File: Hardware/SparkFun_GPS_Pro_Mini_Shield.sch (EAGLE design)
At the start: 23 parts, among them J1 USD_TINY, U1 EM406, U2 TXB0108, U3 AP2112K-3.3V

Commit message: Update file names and library
- Updated file names to follow standard
- Updated library with PROD_ID numbers
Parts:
- J1: value USD_TINY -> MICROSD_TINY; device uSD Socket temp:USD_TINY -> GPS_Pro_Mini_temp:MICROSD_TINY
- U1: value EM406 -> GP735; device SparkFun-Connectors:EM406 -> GPS_Pro_Mini_temp:GP735
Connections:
- net GND: now also U1.GND; no longer U1.GND1
- net GPS_PPS: now also U1.P_CTRL; no longer U1.1PPS
- net V_BATT: now also U1.VBAT; no longer U1.GND2
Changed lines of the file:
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@@
 </classes>
 <parts>
-<part name="J1" library="uSD Socket temp" deviceset="USD_TINY" device=""/>
+<part name="J1" library="GPS_Pro_Mini_temp" deviceset="MICROSD_TINY" device=""/>
 <part name="J2" library="SparkFun-Connectors" deviceset="M12" device="NO_SILK"/>
 <part name="J3" library="SparkFun-Connectors" deviceset="M12" device="NO_SILK"/>
@@
 <part name="GND1" library="SparkFun-Aesthetics" deviceset="GND" device=""/>
 <part name="GND2" library="SparkFun-Aesthetics" deviceset="GND" device=""/>
-<part name="U1" library="SparkFun-Connectors" deviceset="EM406" device=""/>
+<part name="U1" library="GPS_Pro_Mini_temp" deviceset="GP735" device=""/>
 <part name="J4" library="SparkFun-Connectors" deviceset="M06" device="NO_SILK_FEMALE_PTH"/>
 <part name="SUPPLY3" library="SparkFun-Aesthetics" deviceset="3.3V" device=""/>
@@
 </segment>
 <segment>
-<pinref part="U1" gate="G$1" pin="GND1"/>
+<pinref part="U1" gate="G$1" pin="GND"/>
 <wire x1="22.86" y1="88.9" x2="17.78" y2="88.9" width="0.1524" layer="91"/>
 <wire x1="17.78" y1="88.9" x2="17.78" y2="71.12" width="0.1524" layer="91"/>
@@
 </segment>
 <segment>
-<pinref part="U1" gate="G$1" pin="GND2"/>
+<pinref part="U1" gate="G$1" pin="VBAT"/>
 <wire x1="22.86" y1="78.74" x2="20.32" y2="78.74" width="0.1524" layer="91"/>
 <wire x1="20.32" y1="78.74" x2="20.32" y2="93.98" width="0.1524" layer="91"/>
@@
 <net name="GPS_PPS" class="0">
 <segment>
-<pinref part="U1" gate="G$1" pin="1PPS"/>
+<pinref part="U1" gate="G$1" pin="P_CTRL"/>
 <wire x1="22.86" y1="76.2" x2="15.24" y2="76.2" width="0.1524" layer="91"/>
 <label x="15.24" y="76.2" size="1.27" layer="95" rot="R180" xref="yes"/>

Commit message: Updated GPS label
Changed from GPS_PPS to GPS_CTRL
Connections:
- net GPS_PPS renamed GPS_CTRL
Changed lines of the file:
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@@
 </segment>
 </net>
-<net name="GPS_PPS" class="0">
+<net name="GPS_CTRL" class="0">
 <segment>
 <pinref part="U1" gate="G$1" pin="P_CTRL"/>

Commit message: Added board designer name and version number
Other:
- note added: "Alex Wende"
- note added: "v01"
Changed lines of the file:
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@@
 <wire x1="78.74" y1="53.34" x2="78.74" y2="0" width="0.1524" layer="97" style="shortdash"/>
 <wire x1="40.64" y1="53.34" x2="40.64" y2="0" width="0.1524" layer="97" style="shortdash"/>
+<text x="166.878" y="11.43" size="2.54" layer="94">Alex Wende</text>
+<text x="238.76" y="7.62" size="2.54" layer="94">v01</text>
 </plain>
 <instances>

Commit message: Design Review Changes
- Fixed SPI traces
- Moved VIN of regulator to VIN instead of RAW
- Removed jumpers for software/hardware uart with DPDT switch
- Added product name to board
- Replaced coin cell battery with two PTH pins to make the board smaller
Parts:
- removed BAT1: 12MM Coin Cell, SparkFun-Electromechanical:BATTERY12MM
- removed FD3, FD4: FIDUCIALUFIDUCIAL, SparkFun-Aesthetics:FIDUCIALUFIDUCIAL
- removed JP1: JUMPER-PAD-2-NOYES_SILK, SparkFun-Passives:JUMPER-PAD-2-NOYES_SILK
- removed JP2, JP3: JUMPER-PAD-3-2OF3_NC_BY_PASTE, SparkFun-Passives:JUMPER-PAD-3-2OF3_NC_BY_PASTE
- added J5: (no value), SparkFun-Connectors:M021X02_NO_SILK
- added S1: DPDT, SparkFun-Electromechanical:SWITCH-DPDTAYZ0202
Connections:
- removed net HV_CS: U2.B4
- removed net HV_MISO: U2.B1
- removed net HV_MOSI: U2.B3
- removed net HV_SCK: U2.B2
- net 0/RX: now also S1.3; no longer JP2.3
- net 1/TX: now also S1.6; no longer JP3.3
- net 10: now also U2.B8
- net 11: now also U2.B7
- net 12: now also U2.B5
- net 13: now also U2.B6
- net 3.3V: no longer JP1.2
- net 4: now also S1.1; no longer JP2.1
- net 5: now also S1.4; no longer JP3.1
- net 6: now also U2.B1; no longer U2.B6
- net GND: now also J5.1; no longer BAT1.-
- net GPS_CTRL: now also U2.A1; no longer U2.A6
- net GPS_RX: now also J4.4, U2.A3; no longer J4.3, U2.A8
- net GPS_TX: now also J4.3, U2.A2; no longer J4.4, U2.A7
- net RX: now also S1.2, U2.B2; no longer JP2.2, U2.B7
- net SD_CS: now also U2.A8; no longer U2.A4
- net SD_DI: now also U2.A7; no longer U2.A3
- net SD_DO: now also U2.A5; no longer U2.A1
- net SD_SCK: now also U2.A6; no longer U2.A2
- net TX: now also S1.5, U2.B3; no longer JP3.2, U2.B8
- net VCC: now also C5.1, U3.EN, U3.IN
- net VIN: no longer C5.1, U3.EN, U3.IN
- net V_BATT: now also J5.2; no longer BAT1.+, JP1.1
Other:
- note added: "Software/Hardware UART Select"
- note added: "V_BATT : 1.5V - 3.5V"
- note removed: "Software/Hardware UART Jumpers"

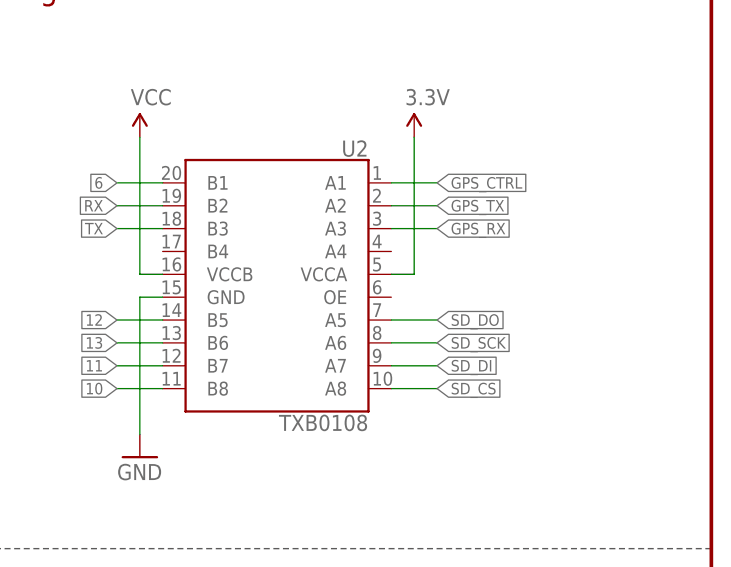
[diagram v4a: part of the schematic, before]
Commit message: QC Changes
- shorted output enable to VCCA
- added note of PCB thickness to tDocu
- added VBATT to bottom silk for 2-pin vbatt header
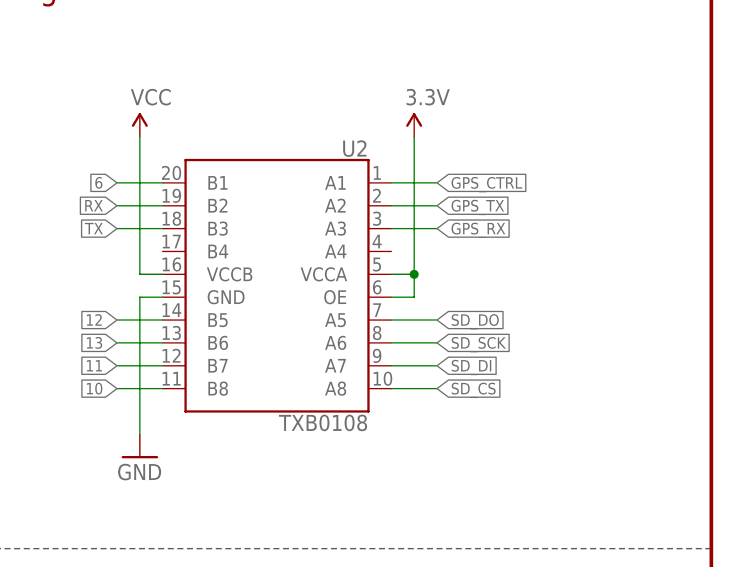
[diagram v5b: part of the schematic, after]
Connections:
- net 3.3V: now also U2.OE
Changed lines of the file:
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@@
 <wire x1="215.9" y1="149.86" x2="215.9" y2="165.1" width="0.1524" layer="91"/>
 <pinref part="SUPPLY7" gate="G$1" pin="3.3V"/>
+<pinref part="U2" gate="G$1" pin="OE"/>
+<wire x1="213.36" y1="147.32" x2="215.9" y2="147.32" width="0.1524" layer="91"/>
+<wire x1="215.9" y1="147.32" x2="215.9" y2="149.86" width="0.1524" layer="91"/>
+<junction x="215.9" y="149.86"/>
 </segment>
 <segment>
